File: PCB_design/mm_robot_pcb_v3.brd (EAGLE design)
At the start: 34 x 46 mm, 35 parts, among them U1 PIC32

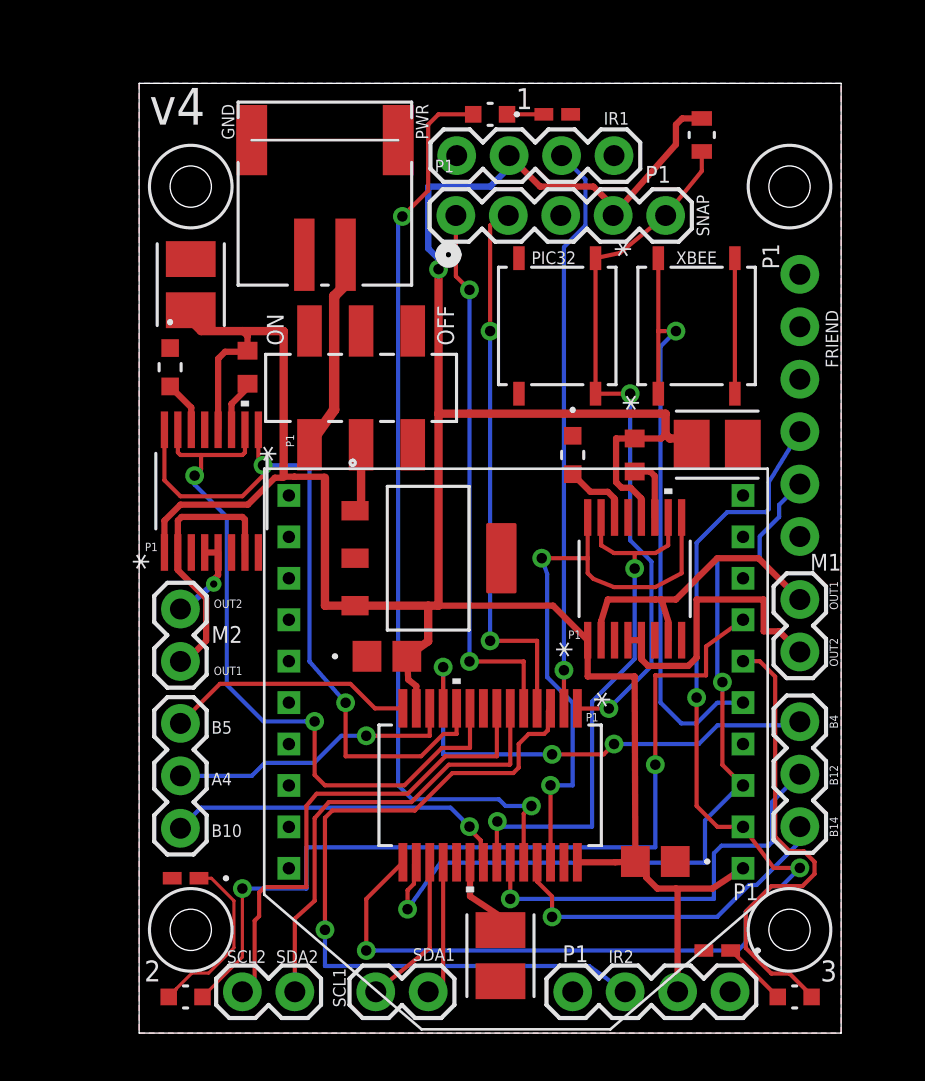
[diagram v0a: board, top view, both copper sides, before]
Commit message: Renamed PCB files so they're numbered correctly
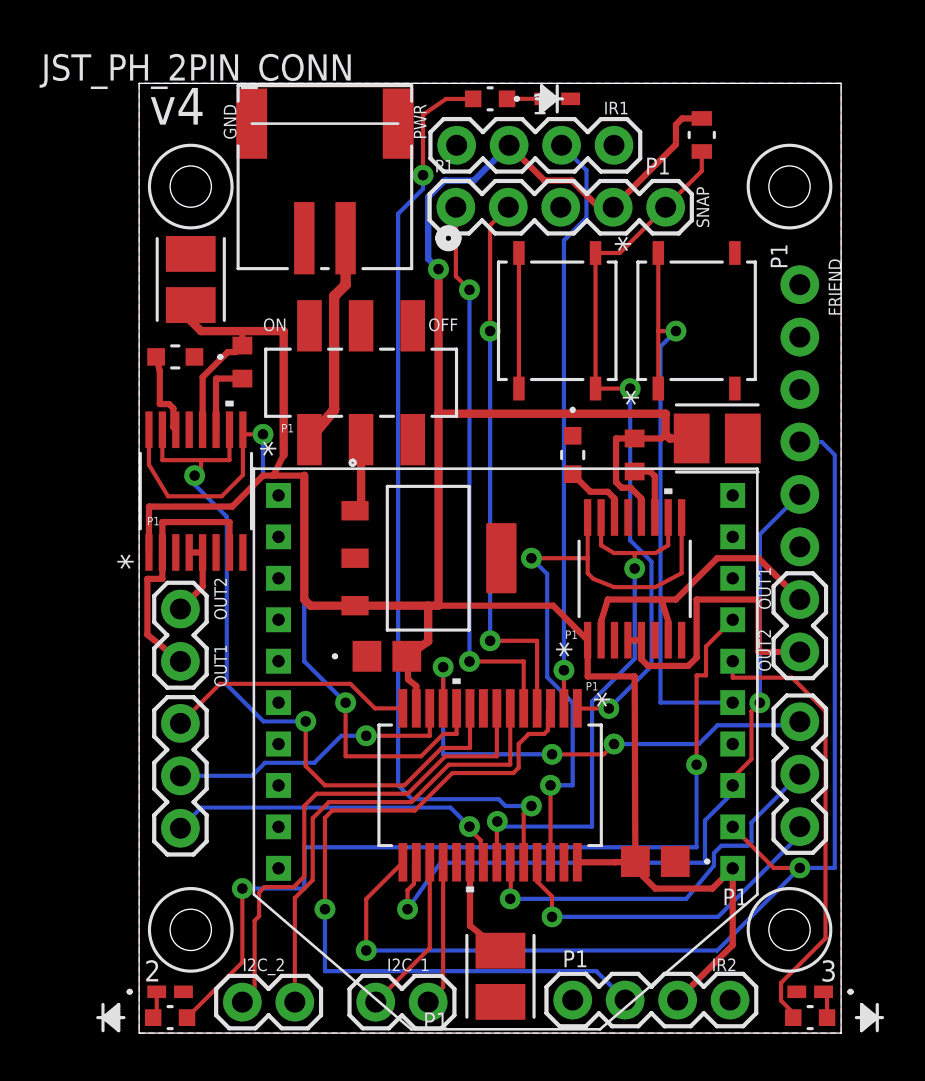
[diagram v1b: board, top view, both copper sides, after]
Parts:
- moved R7 5.55 mm to (1.50, 2.00), turned to 0 degrees
- moved R8 4.92 mm to (32.5, 2.00)
- moved LED2 1.25 mm to (1.50, 0.75)
- moved LED3 1.25 mm to (32.5, 0.75), turned to 180 degrees
- moved C10 1.00 mm to (17.5, 2.75)
- moved JST_PH_2PIN_CONN 0.80 mm to (10.0, 38.5)
- moved DRIVER2 0.75 mm to (2.75, 26.2)
- moved LED1 0.75 mm to (17.0, 45.2)
- moved R6 0.75 mm to (20.2, 45.2)
- moved C2_VINT2 0.56 mm to (1.75, 32.8), turned to 180 degrees
- moved FRIEND 0.50 mm to (32.0, 36.2)
- moved I2C_2 0.50 mm to (5.00, 1.50)
- moved IR1 0.50 mm to (23.0, 43.0)
- moved PCI-PINS4 0.50 mm to (14.0, 1.50)
- moved XBEE_ROBOT 0.50 mm to (17.8, 14.0)
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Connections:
- net RB12-AN12 renamed RP12-AN12
- new net PB_C7: PIC_PB.3, PIC_PB.4
- net GND: no longer PIC_PB.3, PIC_PB.4
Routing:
- net R7: track 8.59 -> 1.32 mm
- net PB_C7: track 0.00 -> 6.57 mm
- net GND: track 6.57 -> 0.00 mm
- net RPB7-PICTX-XBEERX: track 40.5 -> 37.8 mm
- net V+: track 140.9 -> 142.9 mm
- net R8: track 3.22 -> 1.32 mm
- net RPA3-OC3: track 34.3 -> 36.2 mm
- net VINT2: track 2.52 -> 4.14 mm
- net RP12-AN12: track 20.7 -> 19.3 mm
- net XBEE_RESET: track 30.6 -> 29.2 mm
- net VCP2: track 2.55 -> 3.75 mm
- net XBEE_PWM1: track 42.4 -> 43.4 mm
- net VCAP: track 4.08 -> 4.98 mm
- net RPB15-OC1: track 28.9 -> 29.7 mm
- net XBEE_PWM0: track 22.7 -> 21.9 mm
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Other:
- board text added: "I2C_1"
- board text added: "I2C_2"
- board text removed: "A4"
- board text removed: "B10"
- board text removed: "B12"
- board text removed: "B14"
- board text removed: "B4"
- board text removed: "B5"
- board text removed: "M1"
- board text removed: "M2"
- board text removed: "PIC32"
- board text removed: "SCL1"
- board text removed: "SCL2 SDA2"
- board text removed: "SDA1"
- board text removed: "XBEE"
